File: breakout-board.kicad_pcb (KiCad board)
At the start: 2 copper layers, 81 x 47 mm, 19 parts, among them J1 Conn_01x04_Male, J10 Conn_01x02_Male, J2 Conn_01x08_Male, J3 Conn_01x08_Male, J4 Conn_01x02_Male, J5 Conn_02x08_Counter_Clockwise, J6 Conn_01x08_Male, J7 Conn_01x02_Male, J8 Conn_01x02_Male, J9 Conn_01x02_Male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

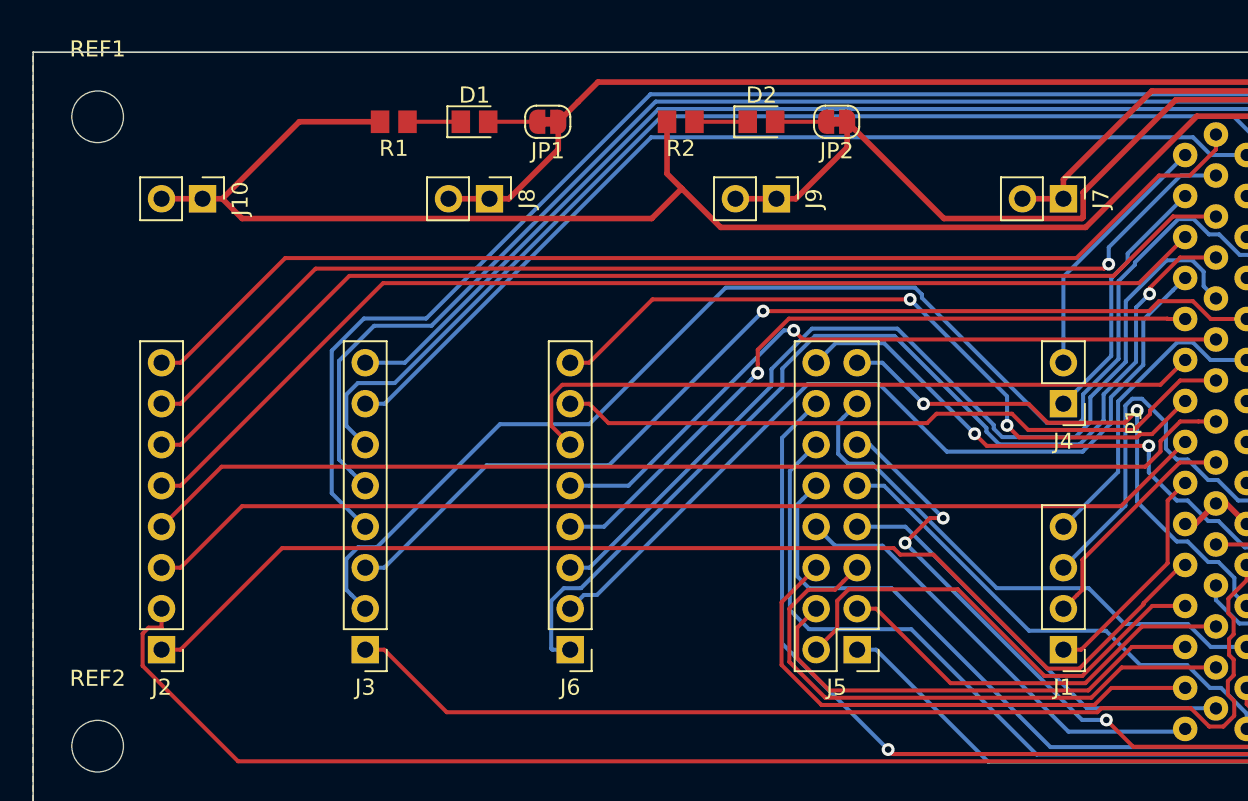
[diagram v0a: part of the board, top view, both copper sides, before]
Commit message: Added a few labels
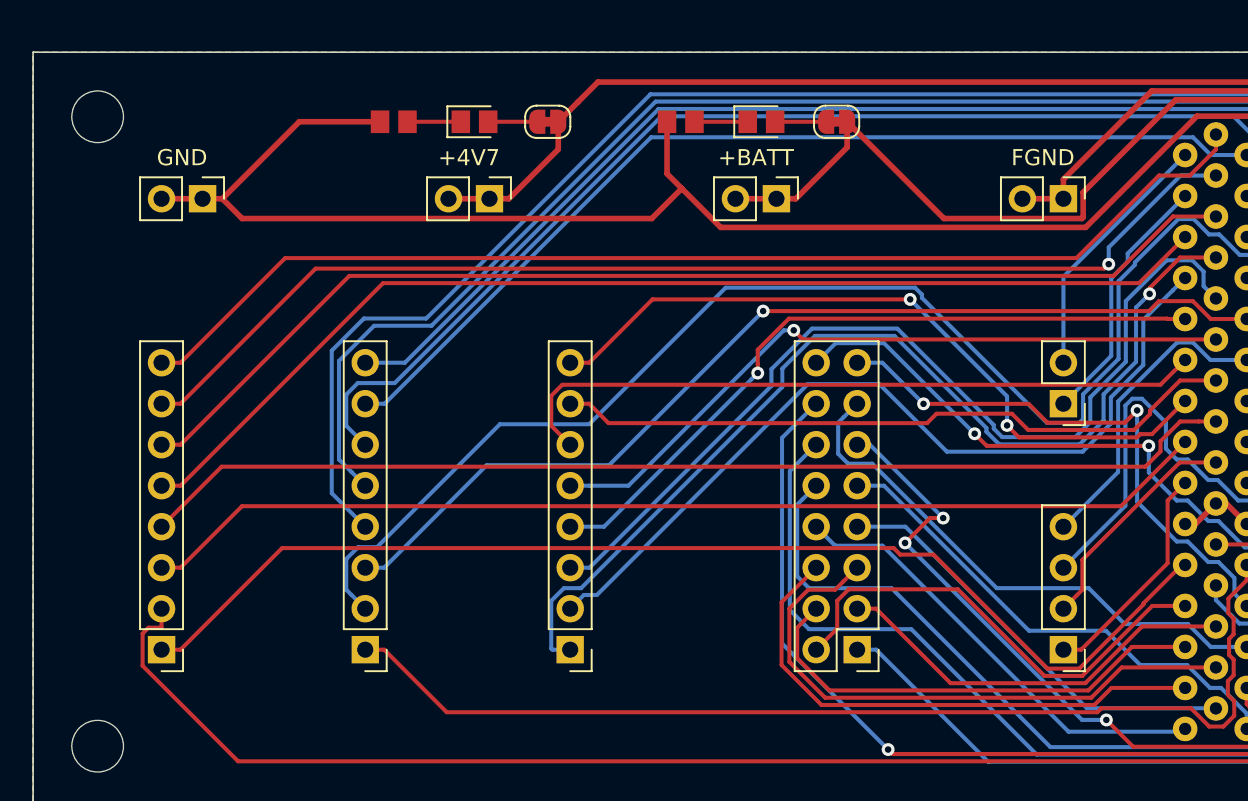
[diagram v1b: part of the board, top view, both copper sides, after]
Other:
- board text added: "+4V7"
- board text added: "+BATT"
- board text added: "FGND"
- board text added: "GND"
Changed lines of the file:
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@@
   (general
     (thickness 1.6)
-    (drawings 6)
+    (drawings 10)
     (tracks 528)
     (zones 0)
@@
   (page A4)
   (layers
-    (0 F.Cu signal)
-    (31 B.Cu signal)
+    (0 F.Cu signal hide)
+    (31 B.Cu signal hide)
     (32 B.Adhes user)
     (33 F.Adhes user)
@@
     (tags "mounting hole 3.2mm no annular m3")
     (attr virtual)
-    (fp_text reference REF1 (at 0 -4.2) (layer F.SilkS)
+    (fp_text reference REF1 (at 0 -4.2) (layer F.SilkS) hide
       (effects (font (size 1 1) (thickness 0.15)))
     )
@@
     (tags "mounting hole 3.2mm no annular m3")
     (attr virtual)
-    (fp_text reference REF2 (at 0 -4.2) (layer F.SilkS)
+    (fp_text reference REF2 (at 0 -4.2) (layer F.SilkS) hide
       (effects (font (size 1 1) (thickness 0.15)))
     )
@@
     (fp_circle (center 0 0) (end 3.45 0) (layer F.CrtYd) (width 0.05))
     (fp_circle (center 0 0) (end 3.2 0) (layer Cmts.User) (width 0.15))
-    (fp_text user %R (at 0.3 0) (layer F.Fab)
+    (fp_text user %R (at 0.3 0) (layer F.Fab) hide
       (effects (font (size 1 1) (thickness 0.15)))
     )
@@
     (tags diode)
     (attr smd)
-    (fp_text reference D1 (at 0 -1.65) (layer F.SilkS)
-      (effects (font (size 1 1) (thickness 0.15)))
-    )
-    (fp_text value LED (at 0 1.65) (layer F.Fab)
+    (fp_text reference D1 (at 0 -1.65) (layer F.SilkS) hide
+      (effects (font (size 1 1) (thickness 0.15)))
+    )
+    (fp_text value LED (at 0 -1.58) (layer F.Fab)
       (effects (font (size 1 1) (thickness 0.15)))
     )
@@
     (tags diode)
     (attr smd)
-    (fp_text reference D2 (at 0 -1.65) (layer F.SilkS)
-      (effects (font (size 1 1) (thickness 0.15)))
-    )
-    (fp_text value LED (at 0 1.65) (layer F.Fab)
-      (effects (font (size 1 1) (thickness 0.15)))
-    )
-    (fp_line (start 1 -0.6) (end -0.7 -0.6) (layer F.Fab) (width 0.1))
-    (fp_line (start -0.7 -0.6) (end -1 -0.3) (layer F.Fab) (width 0.1))
-    (fp_line (start -1 -0.3) (end -1 0.6) (layer F.Fab) (width 0.1))
-    (fp_line (start -1 0.6) (end 1 0.6) (layer F.Fab) (width 0.1))
-    (fp_line (start 1 0.6) (end 1 -0.6) (layer F.Fab) (width 0.1))
-    (fp_line (start 1 -0.96) (end -1.685 -0.96) (layer F.SilkS) (width 0.12))
-    (fp_line (start -1.685 -0.96) (end -1.685 0.96) (layer F.SilkS) (width 0.12))
-    (fp_line (start -1.685 0.96) (end 1 0.96) (layer F.SilkS) (width 0.12))
-    (fp_line (start -1.68 0.95) (end -1.68 -0.95) (layer F.CrtYd) (width 0.05))
-    (fp_line (start -1.68 -0.95) (end 1.68 -0.95) (layer F.CrtYd) (width 0.05))
-    (fp_line (start 1.68 -0.95) (end 1.68 0.95) (layer F.CrtYd) (width 0.05))
-    (fp_line (start 1.68 0.95) (end -1.68 0.95) (layer F.CrtYd) (width 0.05))
+    (fp_text reference D2 (at 0 -1.65) (layer F.SilkS) hide
+      (effects (font (size 1 1) (thickness 0.15)))
+    )
+    (fp_text value LED (at 0 -1.58) (layer F.Fab)
+      (effects (font (size 1 1) (thickness 0.15)))
+    )
     (fp_text user %R (at 0 0) (layer F.Fab)
       (effects (font (size 0.5 0.5) (thickness 0.08)))
     )
+    (fp_line (start 1.68 0.95) (end -1.68 0.95) (layer F.CrtYd) (width 0.05))
+    (fp_line (start 1.68 -0.95) (end 1.68 0.95) (layer F.CrtYd) (width 0.05))
+    (fp_line (start -1.68 -0.95) (end 1.68 -0.95) (layer F.CrtYd) (width 0.05))
+    (fp_line (start -1.68 0.95) (end -1.68 -0.95) (layer F.CrtYd) (width 0.05))
+    (fp_line (start -1.685 0.96) (end 1 0.96) (layer F.SilkS) (width 0.12))
+    (fp_line (start -1.685 -0.96) (end -1.685 0.96) (layer F.SilkS) (width 0.12))
+    (fp_line (start 1 -0.96) (end -1.685 -0.96) (layer F.SilkS) (width 0.12))
+    (fp_line (start 1 0.6) (end 1 -0.6) (layer F.Fab) (width 0.1))
+    (fp_line (start -1 0.6) (end 1 0.6) (layer F.Fab) (width 0.1))
+    (fp_line (start -1 -0.3) (end -1 0.6) (layer F.Fab) (width 0.1))
+    (fp_line (start -0.7 -0.6) (end -1 -0.3) (layer F.Fab) (width 0.1))
+    (fp_line (start 1 -0.6) (end -0.7 -0.6) (layer F.Fab) (width 0.1))
+    (pad 2 smd rect (at 0.85 0) (size 1.15 1.4) (layers F.Cu F.Paste F.Mask)
+      (net 4 "Net-(D2-Pad2)"))
     (pad 1 smd rect (at -0.85 0) (size 1.15 1.4) (layers F.Cu F.Paste F.Mask)
       (net 3 "Net-(D2-Pad1)"))
-    (pad 2 smd rect (at 0.85 0) (size 1.15 1.4) (layers F.Cu F.Paste F.Mask)
-      (net 4 "Net-(D2-Pad2)"))
     (model ${KISYS3DMOD}/LED_SMD.3dshapes/LED_0805_2012Metric.wrl
       (at (xyz 0 0 0))
@@
     (descr "Through hole straight pin header, 1x04, 2.54mm pitch, single row")
     (tags "Through hole pin header THT 1x04 2.54mm single row")
-    (fp_text reference J1 (at 0 -2.33 180) (layer F.SilkS)
+    (fp_text reference J1 (at 0 -2.33 180) (layer F.SilkS) hide
       (effects (font (size 1 1) (thickness 0.15)))
     )
@@
     (descr "Through hole straight pin header, 1x08, 2.54mm pitch, single row")
     (tags "Through hole pin header THT 1x08 2.54mm single row")
-    (fp_text reference J2 (at 0 -2.33 180) (layer F.SilkS)
+    (fp_text reference J2 (at 0 -2.33 180) (layer F.SilkS) hide
       (effects (font (size 1 1) (thickness 0.15)))
     )
@@
     (descr "Through hole straight pin header, 1x08, 2.54mm pitch, single row")
     (tags "Through hole pin header THT 1x08 2.54mm single row")
-    (fp_text reference J3 (at 0 -2.33 180) (layer F.SilkS)
+    (fp_text reference J3 (at 0 -2.33 180) (layer F.SilkS) hide
       (effects (font (size 1 1) (thickness 0.15)))
     )
@@
     (descr "Through hole straight pin header, 1x02, 2.54mm pitch, single row")
     (tags "Through hole pin header THT 1x02 2.54mm single row")
-    (fp_text reference J4 (at 0 -2.33 180) (layer F.SilkS)
+    (fp_text reference J4 (at 0 -2.33 180) (layer F.SilkS) hide
       (effects (font (size 1 1) (thickness 0.15)))
     )
@@
     (descr "Through hole straight pin header, 2x08, 2.54mm pitch, double rows")
     (tags "Through hole pin header THT 2x08 2.54mm double row")
-    (fp_text reference J5 (at 1.27 -2.33 180) (layer F.SilkS)
+    (fp_text reference J5 (at 1.27 -2.33 180) (layer F.SilkS) hide
       (effects (font (size 1 1) (thickness 0.15)))
     )
@@
     (descr "Through hole straight pin header, 1x08, 2.54mm pitch, single row")
     (tags "Through hole pin header THT 1x08 2.54mm single row")
-    (fp_text reference J6 (at 0 -2.33 180) (layer F.SilkS)
+    (fp_text reference J6 (at 0 -2.33 180) (layer F.SilkS) hide
       (effects (font (size 1 1) (thickness 0.15)))
     )
@@
     (descr "Through hole straight pin header, 1x02, 2.54mm pitch, single row")
     (tags "Through hole pin header THT 1x02 2.54mm single row")
-    (fp_text reference J7 (at 0 -2.33 270) (layer F.SilkS)
+    (fp_text reference J7 (at 0 -2.33 270) (layer F.SilkS) hide
       (effects (font (size 1 1) (thickness 0.15)))
     )
@@
     (descr "Through hole straight pin header, 1x02, 2.54mm pitch, single row")
     (tags "Through hole pin header THT 1x02 2.54mm single row")
-    (fp_text reference J8 (at 0 -2.33 270) (layer F.SilkS)
+    (fp_text reference J8 (at 0 -2.33 270) (layer F.SilkS) hide
       (effects (font (size 1 1) (thickness 0.15)))
     )
@@
     (descr "Through hole straight pin header, 1x02, 2.54mm pitch, single row")
     (tags "Through hole pin header THT 1x02 2.54mm single row")
-    (fp_text reference J9 (at 0 -2.33 270) (layer F.SilkS)
+    (fp_text reference J9 (at 0 -2.33 270) (layer F.SilkS) hide
       (effects (font (size 1 1) (thickness 0.15)))
     )
@@
     (descr "Through hole straight pin header, 1x02, 2.54mm pitch, single row")
     (tags "Through hole pin header THT 1x02 2.54mm single row")
-    (fp_text reference J10 (at 0 -2.33 270) (layer F.SilkS)
+    (fp_text reference J10 (at 0 -2.33 270) (layer F.SilkS) hide
       (effects (font (size 1 1) (thickness 0.15)))
     )
@@
     (tags "solder jumper open")
     (attr virtual)
-    (fp_text reference JP1 (at 0 -1.8 180) (layer F.SilkS)
+    (fp_text reference JP1 (at 0 -1.8 180) (layer F.SilkS) hide
       (effects (font (size 1 1) (thickness 0.15)))
     )
@@
     (tags "solder jumper open")
     (attr virtual)
-    (fp_text reference JP2 (at 0 -1.8 180) (layer F.SilkS)
+    (fp_text reference JP2 (at 0 -1.8 180) (layer F.SilkS) hide
       (effects (font (size 1 1) (thickness 0.15)))
     )
@@
     (tags "SHARP PC CONNECTOR HIF6A-60PA-1.27DS")
     (attr virtual)
-    (fp_text reference P1 (at 0 6.35 270) (layer F.SilkS)
+    (fp_text reference P1 (at 0 6.35 270) (layer F.SilkS) hide
       (effects (font (size 1 1) (thickness 0.15)))
     )
@@
     (tags resistor)
     (attr smd)
-    (fp_text reference R1 (at 0 -1.65 180) (layer F.SilkS)
+    (fp_text reference R1 (at 0 -1.65 180) (layer F.SilkS) hide
       (effects (font (size 1 1) (thickness 0.15)))
     )
@@
     (tags resistor)
     (attr smd)
-    (fp_text reference R2 (at 0 -1.65 180) (layer F.SilkS)
+    (fp_text reference R2 (at 0 -1.65 180) (layer F.SilkS) hide
       (effects (font (size 1 1) (thickness 0.15)))
     )
@@
     )
   )
+  (gr_text GND (at 62.23 129.54) (layer F.SilkS)
+    (effects (font (size 1 1) (thickness 0.15)))
+  )
+  (gr_text FGND (at 115.57 129.54) (layer F.SilkS)
+    (effects (font (size 1 1) (thickness 0.15)))
+  )
+  (gr_text +BATT (at 97.79 129.54) (layer F.SilkS)
+    (effects (font (size 1 1) (thickness 0.15)))
+  )
+  (gr_text +4V7 (at 80.01 129.54) (layer F.SilkS)
+    (effects (font (size 1 1) (thickness 0.15)))
+  )
   (dimension 47 (width 0.3) (layer Cmts.User)

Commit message: Various updates
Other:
- board text added: "(13)"
- board text added: "(14)"
- board text added: "(40)"
- board text added: "(49)"
- board text added: "+4V7 LED"
- board text added: "+BATT LED"
- board text added: "AD0"
- board text added: "AD1"
- board text added: "AD10"
- board text added: "AD11"
- board text added: "AD12"
- board text added: "AD13"
- board text added: "AD14"
- board text added: "AD15"
- board text added: "AD2"
- board text added: "AD3"
- board text added: "AD4"
- board text added: "AD5"
- board text added: "AD6"
- board text added: "AD7"
- board text added: "AD8"
- board text added: "AD9"
- board text added: "BF0"
- board text added: "CMTOUT"
- board text added: "D0"
- board text added: "D1"
- board text added: "D2"
- board text added: "D3"
- board text added: "D4"
- board text added: "D5"
- board text added: "D6"
- board text added: "D7"
- board text added: "DME0"
- board text added: "DME1"
- board text added: "INT"
- board text added: "ME1"
- board text added: "NC"
- board text added: "OD"
- board text added: "PB0"
- board text added: "PB1"
- board text added: "PC7"
- board text added: "PU"
- board text added: "PV"
- board text added: "RW"
- board text added: "SHARP PC 60-Pin Connector Breakout Board"
- board text added: "W1"
- board text added: "www.KaiBader.de"
- board text added: "~CMTIN"
- board text added: "~INH."
- board text added: "~WEX"
- board text added: "ΦOS"
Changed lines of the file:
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@@
   (general
     (thickness 1.6)
-    (drawings 10)
+    (drawings 61)
     (tracks 528)
     (zones 0)
@@
   (page A4)
   (layers
-    (0 F.Cu signal hide)
-    (31 B.Cu signal hide)
+    (0 F.Cu signal)
+    (31 B.Cu signal)
     (32 B.Adhes user)
     (33 F.Adhes user)
@@
     )
   )
-  (gr_text GND (at 62.23 129.54) (layer F.SilkS)
-    (effects (font (size 1 1) (thickness 0.15)))
-  )
-  (gr_text FGND (at 115.57 129.54) (layer F.SilkS)
-    (effects (font (size 1 1) (thickness 0.15)))
-  )
-  (gr_text +BATT (at 97.79 129.54) (layer F.SilkS)
-    (effects (font (size 1 1) (thickness 0.15)))
-  )
-  (gr_text +4V7 (at 80.01 129.54) (layer F.SilkS)
-    (effects (font (size 1 1) (thickness 0.15)))
-  )
+  (gr_text www.KaiBader.de (at 91.44 168.529) (layer F.SilkS)
+    (effects (font (size 1 1) (thickness 0.15)))
+  )
+  (gr_text "+4V7 LED" (at 80.01 125.095) (layer F.SilkS)
+    (effects (font (size 1 1) (thickness 0.15)))
+  )
+  (gr_text "+BATT LED" (at 97.79 125.095) (layer F.SilkS)
+    (effects (font (size 1 1) (thickness 0.15)))
+  )
+  (gr_text NC (at 120.65 162.56) (layer F.SilkS)
+    (effects (font (size 1 1) (thickness 0.15)))
+  )
+  (gr_text "SHARP PC 60-Pin Connector Breakout Board" (at 91.44 166.37) (layer F.SilkS)
+    (effects (font (size 1.5 1.5) (thickness 0.3)))
+  )
+  (gr_text "(13)" (at 120.65 160.02) (layer F.SilkS)
+    (effects (font (size 1 1) (thickness 0.15)))
+  )
+  (gr_text "(14)" (at 120.65 157.48) (layer F.SilkS)
+    (effects (font (size 1 1) (thickness 0.15)))
+  )
+  (gr_text "(40)" (at 120.65 154.94) (layer F.SilkS)
+    (effects (font (size 1 1) (thickness 0.15)))
+  )
+  (gr_text ~CMTIN (at 116.84 147.32) (layer F.SilkS)
+    (effects (font (size 1 1) (thickness 0.15)))
+  )
+  (gr_text CMTOUT (at 116.84 139.7) (layer F.SilkS)
+    (effects (font (size 1 1) (thickness 0.15)))
+  )
+  (gr_text "(49)" (at 120.65 152.4) (layer F.SilkS)
+    (effects (font (size 1 1) (thickness 0.15)))
+  )
+  (gr_text AD0 (at 107.95 160.02) (layer F.SilkS)
+    (effects (font (size 1 1) (thickness 0.15)))
+  )
+  (gr_text AD2 (at 107.95 157.48) (layer F.SilkS)
+    (effects (font (size 1 1) (thickness 0.15)))
+  )
+  (gr_text AD4 (at 107.95 154.94) (layer F.SilkS)
+    (effects (font (size 1 1) (thickness 0.15)))
+  )
+  (gr_text AD6 (at 107.95 152.4) (layer F.SilkS)
+    (effects (font (size 1 1) (thickness 0.15)))
+  )
+  (gr_text AD8 (at 107.95 149.86) (layer F.SilkS)
+    (effects (font (size 1 1) (thickness 0.15)))
+  )
+  (gr_text AD10 (at 107.95 147.32) (layer F.SilkS)
+    (effects (font (size 1 1) (thickness 0.15)))
+  )
+  (gr_text AD12 (at 107.95 144.78) (layer F.SilkS)
+    (effects (font (size 1 1) (thickness 0.15)))
+  )
+  (gr_text AD14 (at 107.95 142.24) (layer F.SilkS)
+    (effects (font (size 1 1) (thickness 0.15)))
+  )
+  (gr_text AD1 (at 97.79 160.02) (layer F.SilkS)
+    (effects (font (size 1 1) (thickness 0.15)))
+  )
+  (gr_text AD3 (at 97.79 157.48) (layer F.SilkS)
+    (effects (font (size 1 1) (thickness 0.15)))
+  )
+  (gr_text AD5 (at 97.79 154.94) (layer F.SilkS)
+    (effects (font (size 1 1) (thickness 0.15)))
+  )
+  (gr_text AD7 (at 97.79 152.4) (layer F.SilkS)
+    (effects (font (size 1 1) (thickness 0.15)))
+  )
+  (gr_text AD9 (at 97.79 149.86) (layer F.SilkS)
+    (effects (font (size 1 1) (thickness 0.15)))
+  )
+  (gr_text AD11 (at 97.79 147.32) (layer F.SilkS)
+    (effects (font (size 1 1) (thickness 0.15)))
+  )
+  (gr_text AD13 (at 97.79 144.78) (layer F.SilkS)
+    (effects (font (size 1 1) (thickness 0.15)))
+  )
+  (gr_text AD15 (at 97.79 142.24) (layer F.SilkS)
+    (effects (font (size 1 1) (thickness 0.15)))
+  )
+  (gr_text D0 (at 90.17 160.02) (layer F.SilkS)
+    (effects (font (size 1 1) (thickness 0.15)))
+  )
+  (gr_text D1 (at 90.17 157.48) (layer F.SilkS)
+    (effects (font (size 1 1) (thickness 0.15)))
+  )
+  (gr_text D2 (at 90.17 154.94) (layer F.SilkS)
+    (effects (font (size 1 1) (thickness 0.15)))
+  )
+  (gr_text D3 (at 90.17 152.4) (layer F.SilkS)
+    (effects (font (size 1 1) (thickness 0.15)))
+  )
+  (gr_text D4 (at 90.17 149.86) (layer F.SilkS)
+    (effects (font (size 1 1) (thickness 0.15)))
+  )
+  (gr_text D5 (at 90.17 147.32) (layer F.SilkS)
+    (effects (font (size 1 1) (thickness 0.15)))
+  )
+  (gr_text D6 (at 90.17 144.78) (layer F.SilkS)
+    (effects (font (size 1 1) (thickness 0.15)))
+  )
+  (gr_text D7 (at 90.17 142.24) (layer F.SilkS)
+    (effects (font (size 1 1) (thickness 0.15)))
+  )
+  (gr_text PB1 (at 77.47 160.02) (layer F.SilkS)
+    (effects (font (size 1 1) (thickness 0.15)))
+  )
+  (gr_text BF0 (at 77.47 157.48) (layer F.SilkS)
+    (effects (font (size 1 1) (thickness 0.15)))
+  )
+  (gr_text ΦOS (at 77.47 154.94) (layer F.SilkS)
+    (effects (font (size 1 1) (thickness 0.15)))
+  )
+  (gr_text DME0 (at 77.47 152.4) (layer F.SilkS)
+    (effects (font (size 1 1) (thickness 0.15)))
+  )
+  (gr_text RW (at 77.47 149.86) (layer F.SilkS)
+    (effects (font (size 1 1) (thickness 0.15)))
+  )
+  (gr_text DME1 (at 77.47 147.32) (layer F.SilkS)
+    (effects (font (size 1 1) (thickness 0.15)))
+  )
+  (gr_text ME1 (at 77.47 144.78) (layer F.SilkS)
+    (effects (font (size 1 1) (thickness 0.15)))
+  )
+  (gr_text OD (at 77.47 142.24) (layer F.SilkS)
+    (effects (font (size 1 1) (thickness 0.15)))
+  )
+  (gr_text PB0 (at 64.77 160.02) (layer F.SilkS)
+    (effects (font (size 1 1) (thickness 0.15)))
+  )
+  (gr_text PC7 (at 64.77 157.48) (layer F.SilkS)
+    (effects (font (size 1 1) (thickness 0.15)))
+  )
+  (gr_text PV (at 64.77 154.94) (layer F.SilkS)
+    (effects (font (size 1 1) (thickness 0.15)))
+  )
+  (gr_text PU (at 64.77 152.4) (layer F.SilkS)
+    (effects (font (size 1 1) (thickness 0.15)))
+  )
+  (gr_text ~INH. (at 64.77 149.86) (layer F.SilkS)
+    (effects (font (size 1 1) (thickness 0.15)))
+  )
+  (gr_text ~WEX (at 64.77 147.32) (layer F.SilkS)
+    (effects (font (size 1 1) (thickness 0.15)))
+  )
+  (gr_text W1 (at 64.77 144.78) (layer F.SilkS)
+    (effects (font (size 1 1) (thickness 0.15)))
+  )
+  (gr_text INT (at 64.77 142.24) (layer F.SilkS)
+    (effects (font (size 1 1) (thickness 0.15)))
+  )
+  (gr_text GND (at 62.23 135.255) (layer F.SilkS)
+    (effects (font (size 1 1) (thickness 0.15)))
+  )
+  (gr_text FGND (at 115.57 135.255) (layer F.SilkS)
+    (effects (font (size 1 1) (thickness 0.15)))
+  )
+  (gr_text +BATT (at 97.79 135.255) (layer F.SilkS)
+    (effects (font (size 1 1) (thickness 0.15)))
+  )
+  (gr_text +4V7 (at 80.01 135.255) (layer F.SilkS)
+    (effects (font (size 1 1) (thickness 0.15)))
+  )
